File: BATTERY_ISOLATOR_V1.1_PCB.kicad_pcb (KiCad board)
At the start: 2 copper layers, 56 x 50 mm, 42 parts, among them J23 CAN 1, J3 PROG, Q1 AO3400A, Q2 AO3400A, Q3 DMTH4008LPS-13, Q4 DMTH4008LPS-13, Q5 DMTH4008LPS-13, Q6 DMTH4008LPS-13, U1 STM32F042F6Px, U2 ACS724xLCTR-30AB, U3 UA78M33QDCYRQ1, U4 UCC27517DBVR, U5 MCP2551-I-SN, Y2 HSE

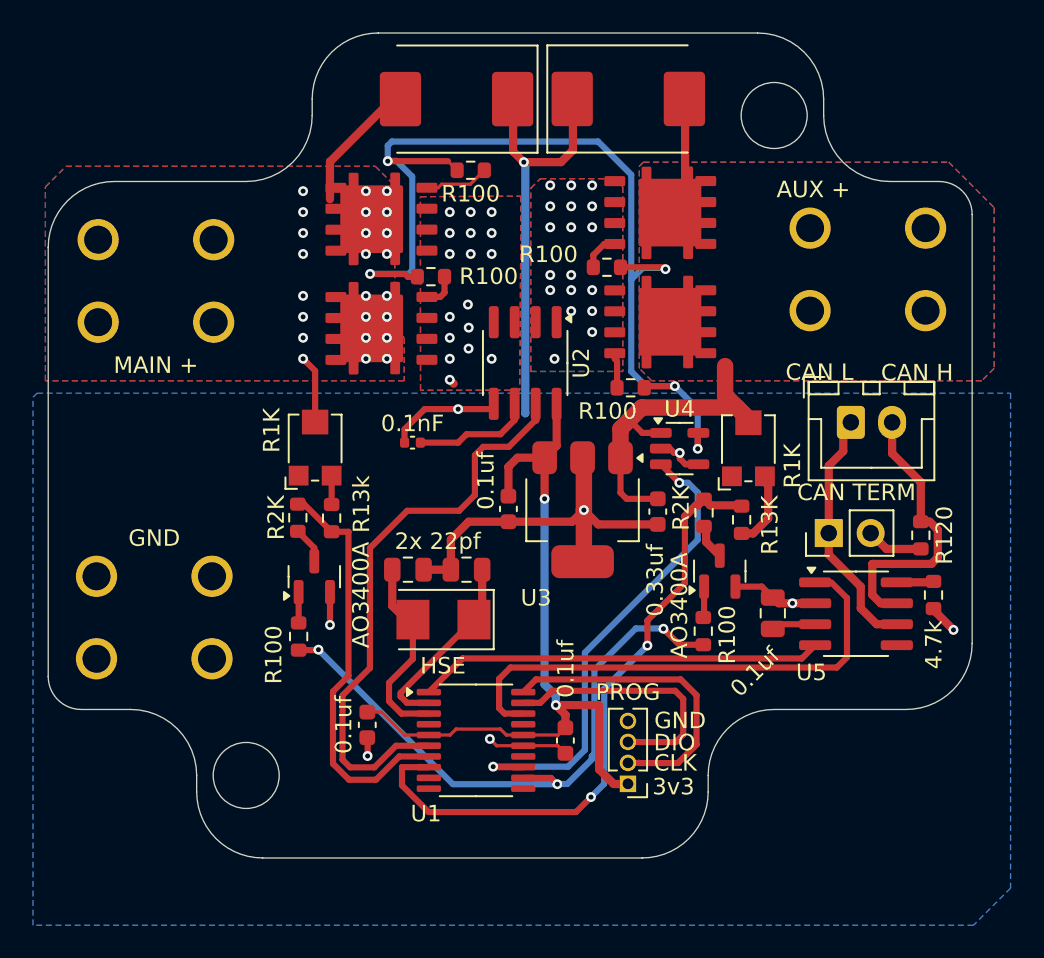
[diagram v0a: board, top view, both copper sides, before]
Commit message: Added bicolor LED and Switch 3V3 source to 12V Main
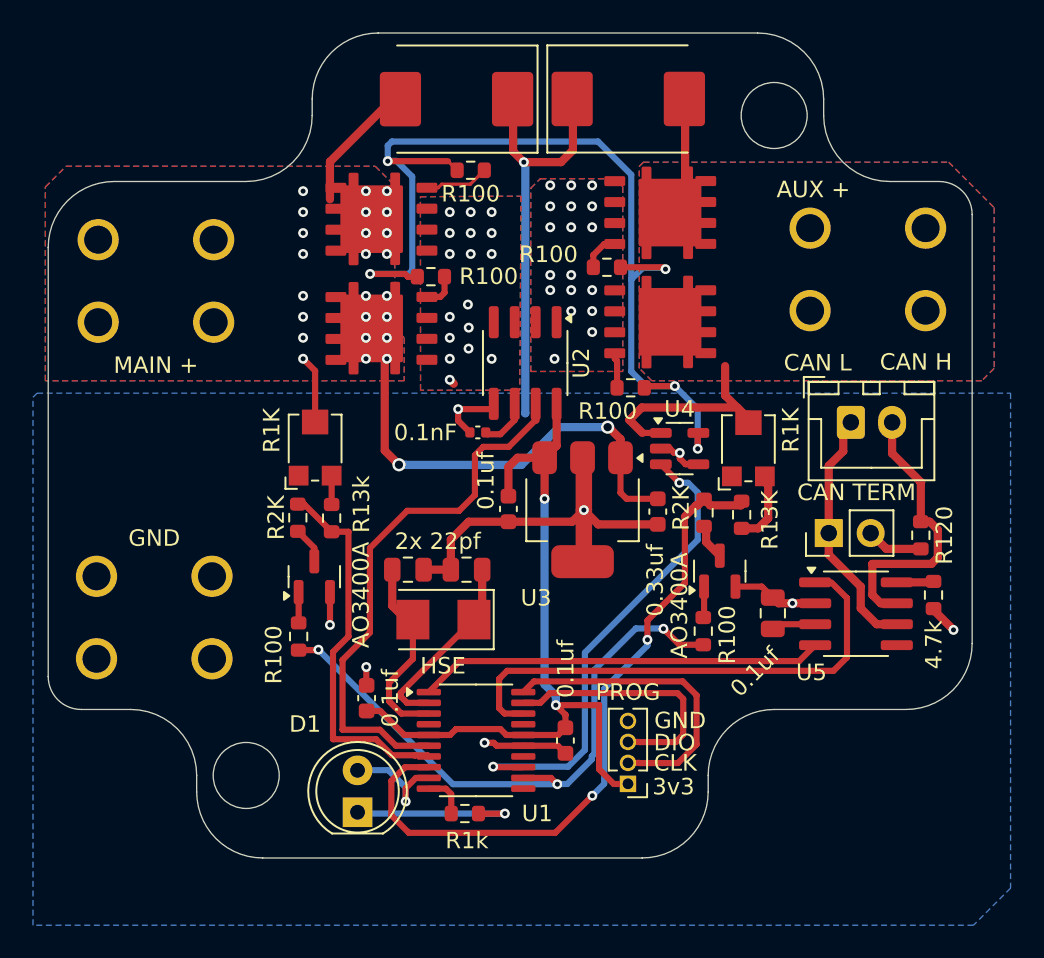
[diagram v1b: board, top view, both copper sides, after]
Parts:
- added D1: LED_Dual_Bidirectional, LED_THT:LED_D5.0mm, F.Cu at (126.1, 113.3)
- added R13: R1k, Resistor_SMD:R_0603_1608Metric, F.Cu at (132.6, 113.4)
- moved C15 4.01 mm to (133.4, 90.3)
- moved C9 1.62 mm to (126.7, 106.4), turned to 90 degrees
- moved R11 0.30 mm to (149.4, 95.3)
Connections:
- C10 pad 1: 12V_AUX -> 12V_MAIN
- U1 pad 10: unconnected-(U1-PA4-Pad10) -> LEDB
- U1 pad 9: unconnected-(U1-PA3-Pad9) -> LEDA
- U3 pad 1: 12V_AUX -> 12V_MAIN
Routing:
- net 12V_MAIN: track 12.3 -> 39.4 mm, vias 24 -> 26
- net Net-(D1-KA): track 0.00 -> 10.6 mm, vias 0 -> 1
- net 12V_AUX: track 28.1 -> 21.0 mm
- net LEDA: track 0.00 -> 6.68 mm, vias 0 -> 1
- net Net-(U2-FILTER): track 7.26 -> 3.14 mm
- net AUX_VDIV_SENSE: track 38.6 -> 41.8 mm
- net LEDB: track 0.00 -> 2.68 mm
- net GND: track 74.6 -> 72.0 mm
- net CSENSE: track 35.1 -> 33.0 mm
- net MAIN_VDIV_SENSE: track 25.0 -> 23.0 mm
